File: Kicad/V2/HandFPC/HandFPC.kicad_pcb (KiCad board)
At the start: 2 copper layers, 25 parts, among them J10 SPI_LED, J2 JST_LED_SPI_5V_GND, J3 JST_LED_SPI_5V_GND, J4 JST_LED_SPI_5V_GND, J5 JST_LED_SPI_5V_GND, J6 JST_LED_SPI_5V_GND, J7 SPI_LED, J8 SPI_LED, J9 SPI_LED, U1 ICM-42688-P_I2C, U2 Hall Sensor DRV5023

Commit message: add edgecut for testing
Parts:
- moved J2 147.1 mm to (52.3, 183.0)
- moved FSR5 134.0 mm to (184.3, 97.4), turned to -90 degrees
- moved J3 130.2 mm to (58.8, 173.5)
- moved J4 124.7 mm to (70.6, 173.4)
- moved J5 123.6 mm to (82.0, 176.6)
- moved J6 123.1 mm to (95.3, 178.0)
- moved J10 122.8 mm to (166.1, 45.1), turned to -90 degrees
- moved C4 119.4 mm to (110.2, 152.1), turned to -90 degrees
- moved C1 113.3 mm to (93.5, 137.8), turned to -90 degrees
- moved C2 113.0 mm to (89.3, 141.5)
- moved U1 109.2 mm to (89.3, 137.6)
- moved J9 107.6 mm to (142.9, 10.5), turned to 180 degrees
- moved FSR1 106.9 mm to (17.5, 137.7)
- moved FSR4 103.0 mm to (165.8, 57.3), turned to 90 degrees
- moved C3 102.6 mm to (89.2, 133.4)
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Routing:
- net GND: track 0.00 -> 10.8 mm
- net +3.3V: track 0.00 -> 9.96 mm
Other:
- board outline added: 197.6 x 206 mm

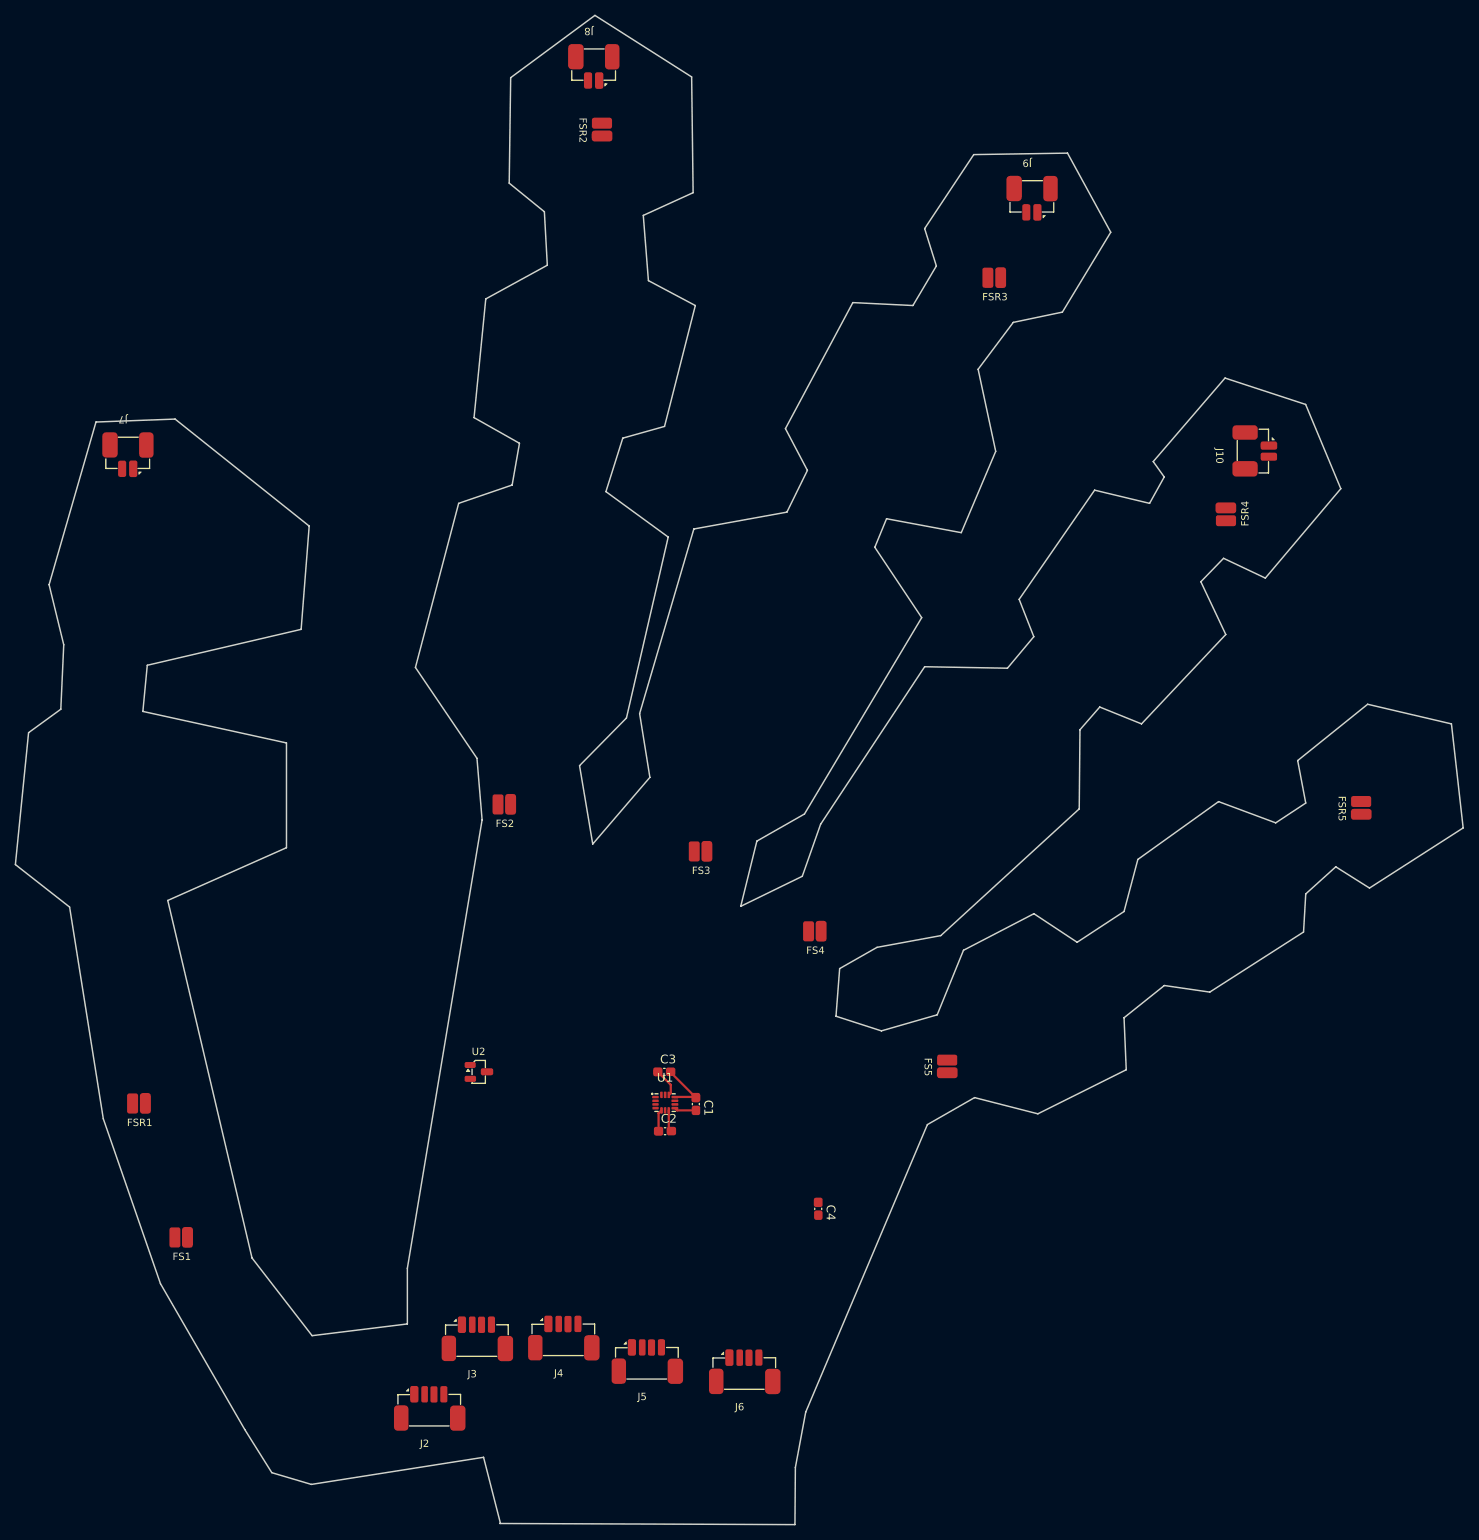
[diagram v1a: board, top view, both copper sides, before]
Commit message: start handfpc routing
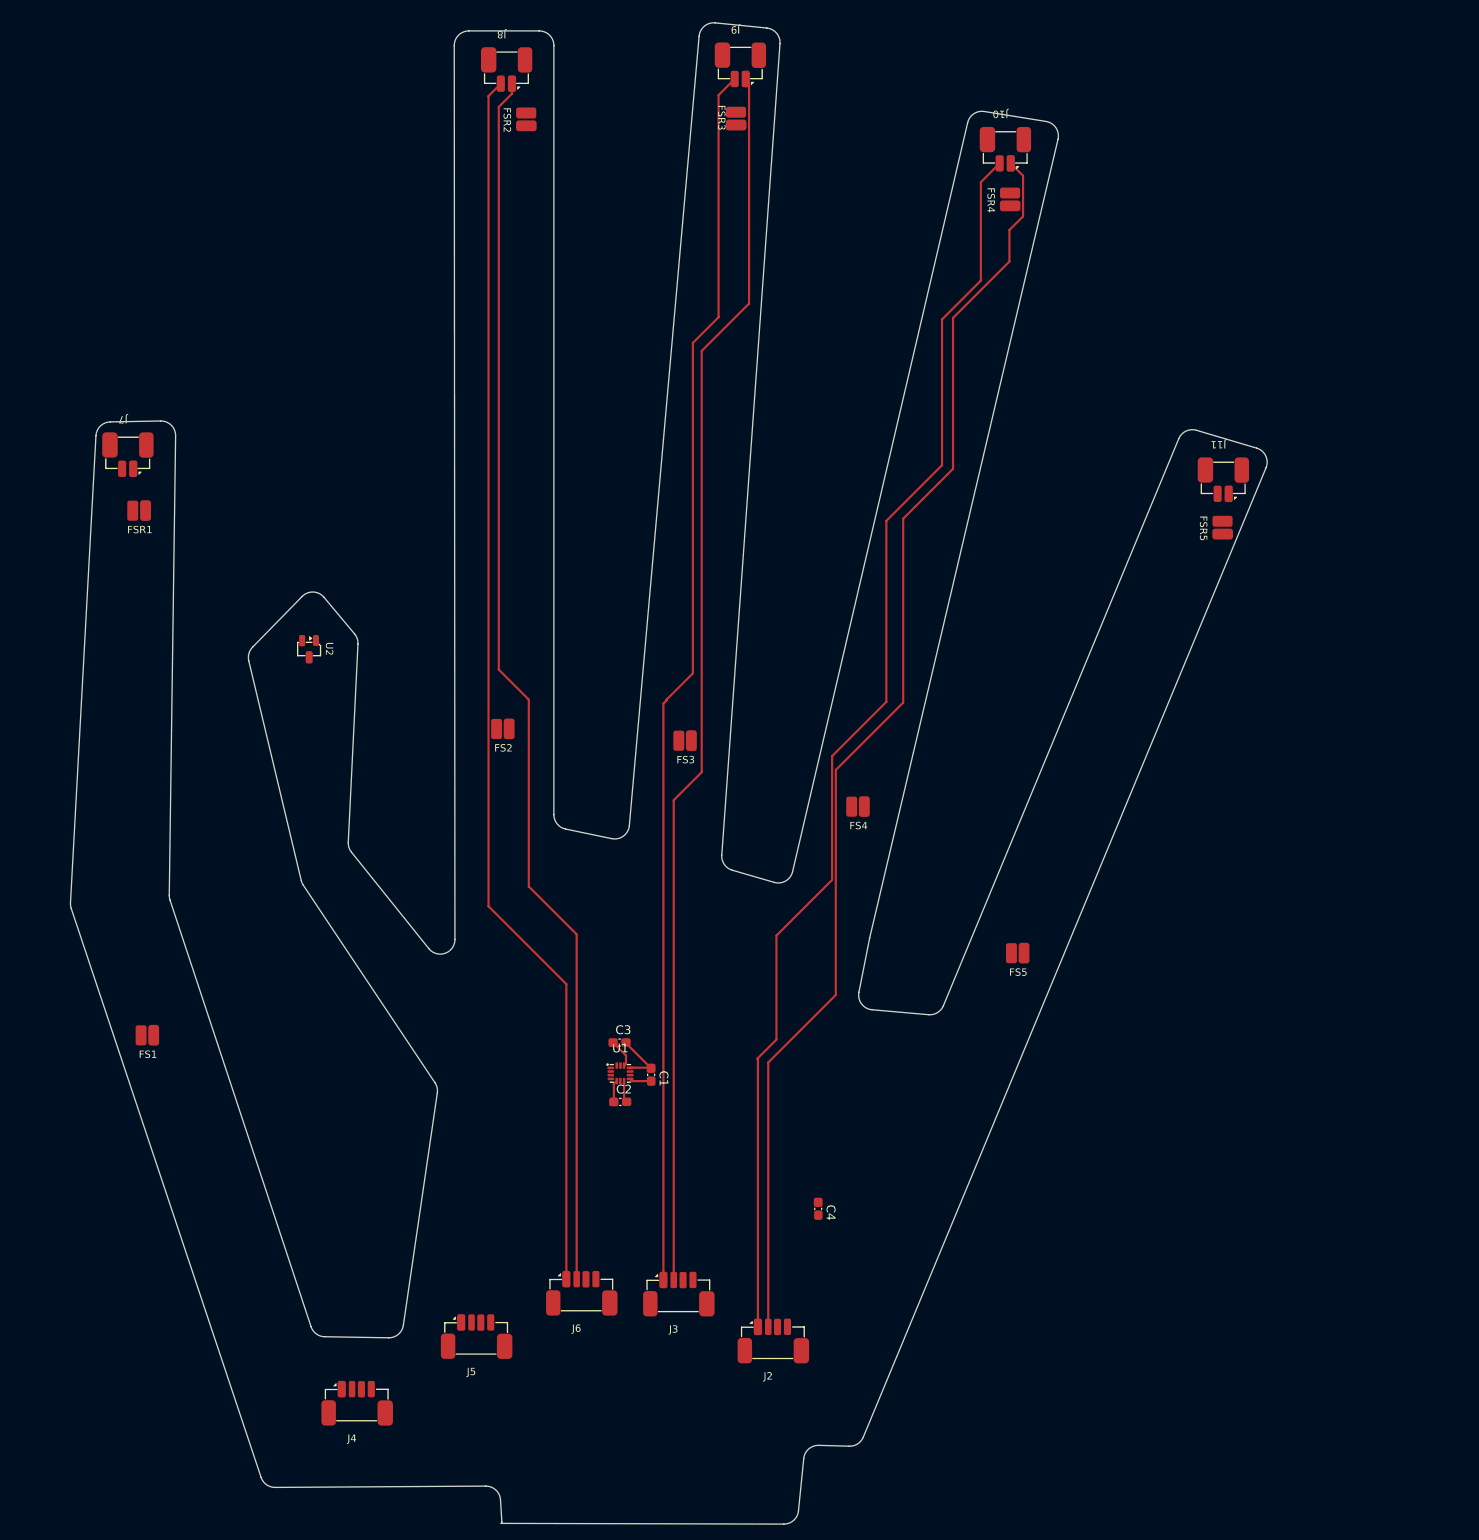
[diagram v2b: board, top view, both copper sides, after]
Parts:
- added J11: JST_SPI_LED_Out_Little, MyGlove:FPC_JST_Conn_GH_2x1.25mm, F.Cu at (169.0, 48.9)
- J10: value SPI_LED -> JST_SPI_LED_Out_Ring
- J2: value JST_LED_SPI_5V_GND -> JST_LED_SPI_In_Little
- J3: value JST_LED_SPI_5V_GND -> JST_LED_SPI_In_Ring
- J4: value JST_LED_SPI_5V_GND -> JST_LED_SPI_In_Thumb
- J5: value JST_LED_SPI_5V_GND -> JST_LED_SPI_In_Index
- J6: value JST_LED_SPI_5V_GND -> JST_LED_SPI_In_Major
- J7: value SPI_LED -> JST_SPI_LED_Out_Thumb
- J8: value SPI_LED -> JST_SPI_LED_Out_Index
- J9: value SPI_LED -> JST_SPI_LED_Out_Major
- moved FSR1 80.9 mm to (17.5, 56.8)
- moved U2 62.2 mm to (40.7, 75.7), turned to -90 degrees
- moved FSR4 52.1 mm to (136.4, 14.3), turned to -90 degrees
- moved J10 49.3 mm to (139.3, 3.84), turned to 180 degrees
- moved J2 47.8 mm to (99.2, 173.8)
- moved J9 43.8 mm to (103.1, -7.68)
- moved FSR5 42.7 mm to (165.4, 59.1)
- moved FSR3 41.4 mm to (99.0, 3.30), turned to -90 degrees
- moved J4 29.6 mm to (42.4, 182.3)
- moved J3 28.2 mm to (86.3, 167.4)
- moved FS1 28.0 mm to (18.7, 128.4)
- moved J6 24.7 mm to (73.0, 167.3)
- moved J5 23.5 mm to (58.7, 173.2)
- moved FS5 18.2 mm to (137.4, 117.2), turned to 0 degrees
- moved FS4 18.0 mm to (115.7, 97.2)
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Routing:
- net Net-(J10-Pad1): track 0.00 -> 173.9 mm
- net Net-(J10-Pad2): track 0.00 -> 172.5 mm
- net Net-(J3-Pad2): track 0.00 -> 168.4 mm
- net Net-(J6-Pad2): track 0.00 -> 168.3 mm
- net Net-(J6-Pad1): track 0.00 -> 168.3 mm
- net Net-(J3-Pad1): track 0.00 -> 167.9 mm
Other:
- board size 197.6 x 206 mm -> 163.3 x 204.9 mm

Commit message: add routing
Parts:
- added J1: FPC_Conn, MyGlove:FPC_Conn_24_GoldFinger, F.Cu at (126.0, 226.9)
- FS1, FS2, FS3, FS4, FS5: moved to B.Cu
- moved C4 81.4 mm to (56.8, 90.6), turned to 180 degrees
- moved J4 70.3 mm to (109.5, 203.0), turned to -90 degrees
- moved FSR1 66.8 mm to (39.8, 119.7), turned to 135 degrees
- moved J7 65.4 mm to (33.7, 109.3), turned to 0 degrees
- moved FS1 59.4 mm to (52.8, 177.0), turned to -120 degrees
- moved J2 57.4 mm to (150.4, 199.6), turned to 135 degrees
- moved J6 56.2 mm to (124.8, 189.0), turned to 180 degrees
- moved J3 55.5 mm to (137.3, 189.2), turned to 180 degrees
- moved FSR2 54.7 mm to (80.1, 57.2), turned to -45 degrees
- moved J8 53.4 mm to (71.1, 46.4), turned to 0 degrees
- moved J5 52.7 mm to (108.1, 191.6), turned to -135 degrees
- moved J9 44.7 mm to (103.3, 37.0), turned to 0 degrees
- moved FSR3 43.0 mm to (108.6, 45.2), turned to -45 degrees
- moved U1 41.5 mm to (117.3, 157.3), turned to 180 degrees
- moved C1 41.1 mm to (121.4, 156.8), turned to 180 degrees
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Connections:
- C4 pad 1: 5V -> +3.3V
- FS1 pad 2: 5V -> +3.3V
- FS2 pad 2: 5V -> +3.3V
- FS3 pad 2: 5V -> +3.3V
- FS4 pad 2: 5V -> +3.3V
- FS5 pad 2: 5V -> +3.3V
- FSR1 pad 2: 5V -> +3.3V
- FSR2 pad 2: 5V -> +3.3V
- FSR3 pad 2: 5V -> +3.3V
- FSR4 pad 2: 5V -> +3.3V
- FSR5 pad 2: 5V -> +3.3V
- U1 pad 1: unconnected-(U1-AP_AD0-Pad1) -> GND
- U2 pad 1: 5V -> +3.3V
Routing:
- net +3.3V: track 9.96 -> 677.5 mm, vias 0 -> 19
- net /FSR_Index/TouchADC: track 0.00 -> 233.2 mm
- net /FSR_Middle/TouchADC: track 0.00 -> 226.3 mm
- net /FSR_Ring/TouchADC: track 0.00 -> 197.9 mm
- net /Flex_Index/FlexADC: track 0.00 -> 184.0 mm, vias 0 -> 1
- net /FSR_Little/TouchADC: track 0.00 -> 176.6 mm
- net /Flex_Middle/FlexADC: track 0.00 -> 165.3 mm, vias 0 -> 1
- net Net-(J5-Pad2): track 0.00 -> 143.6 mm
- net Net-(J5-Pad1): track 0.00 -> 142.5 mm
- net /Flex_Ring/FlexADC: track 0.00 -> 141.8 mm, vias 0 -> 1
- net /Flex_Little/FlexADC: track 0.00 -> 124.9 mm, vias 0 -> 1
- net GND: track 10.8 -> 135.2 mm, vias 0 -> 17
- net 5VL: track 0.00 -> 82.1 mm
- net /IMU_1/IMU_I2C_SDA: track 0.00 -> 70.3 mm, vias 0 -> 2
- net /IMU_1/IMU_I2C_SCL: track 0.00 -> 70.2 mm, vias 0 -> 2
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- added copper zone on B.Cu, net GND
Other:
- board size 163.3 x 204.9 mm -> 144.5 x 199.6 mm

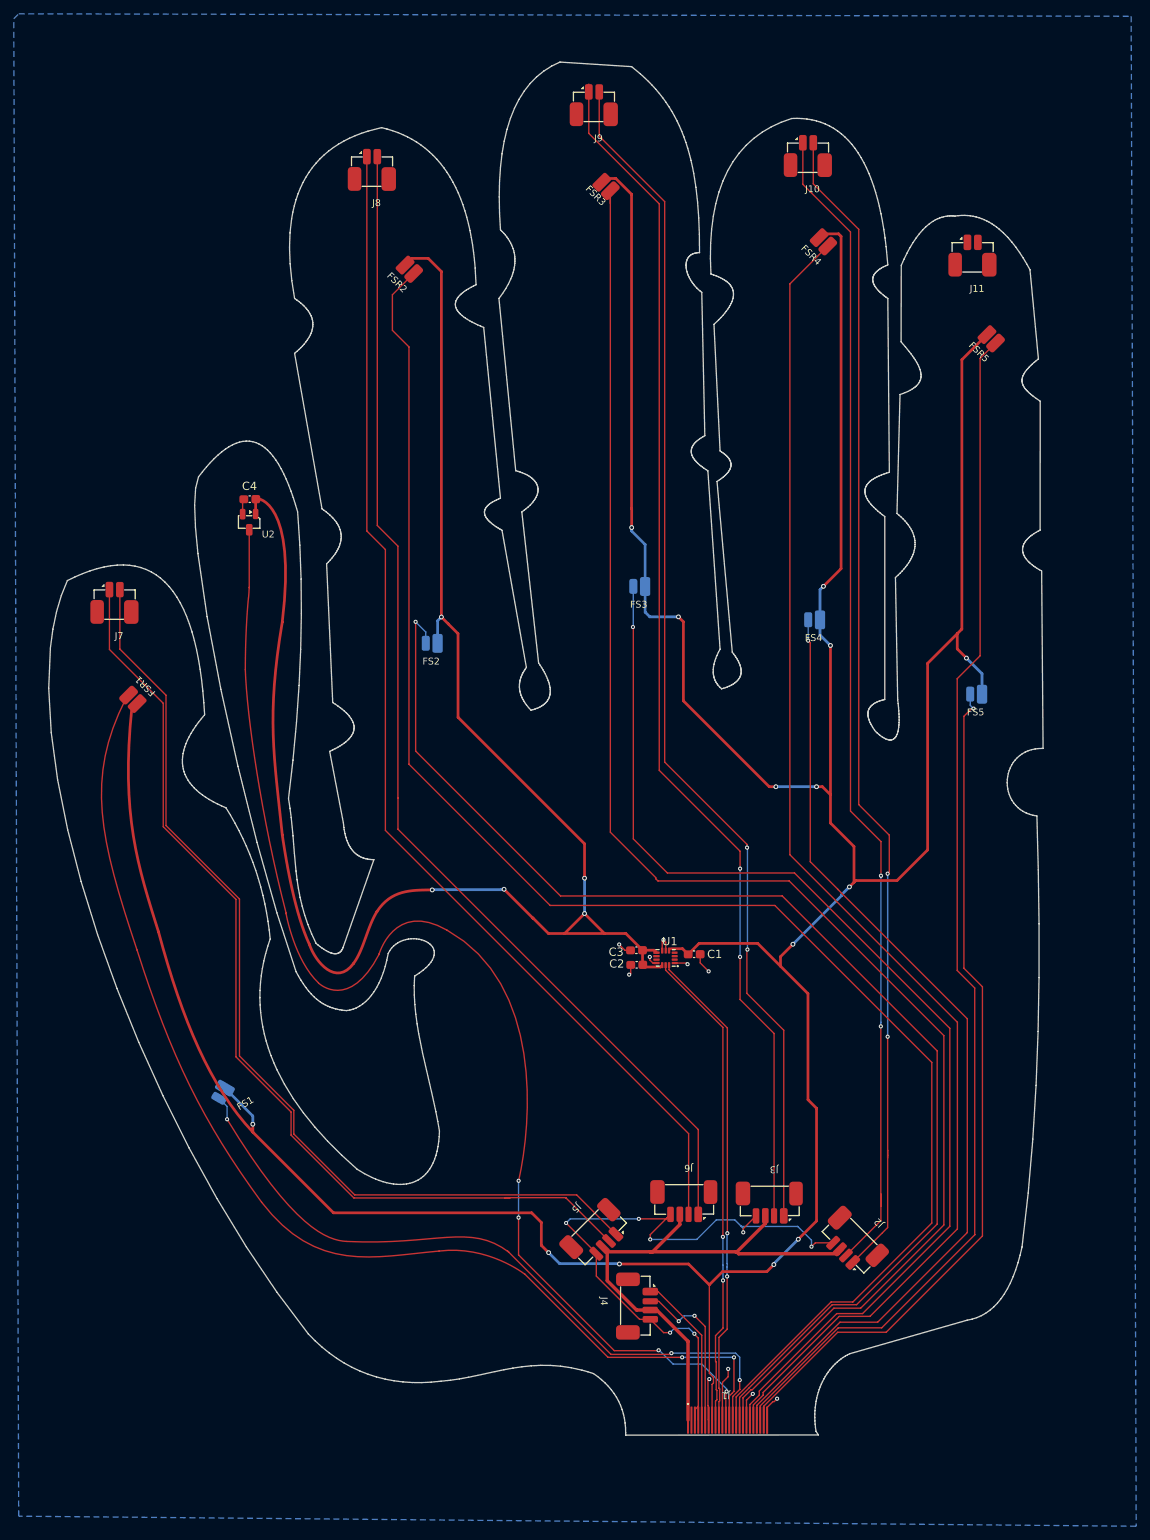
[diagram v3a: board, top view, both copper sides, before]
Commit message: add upper gnd pour
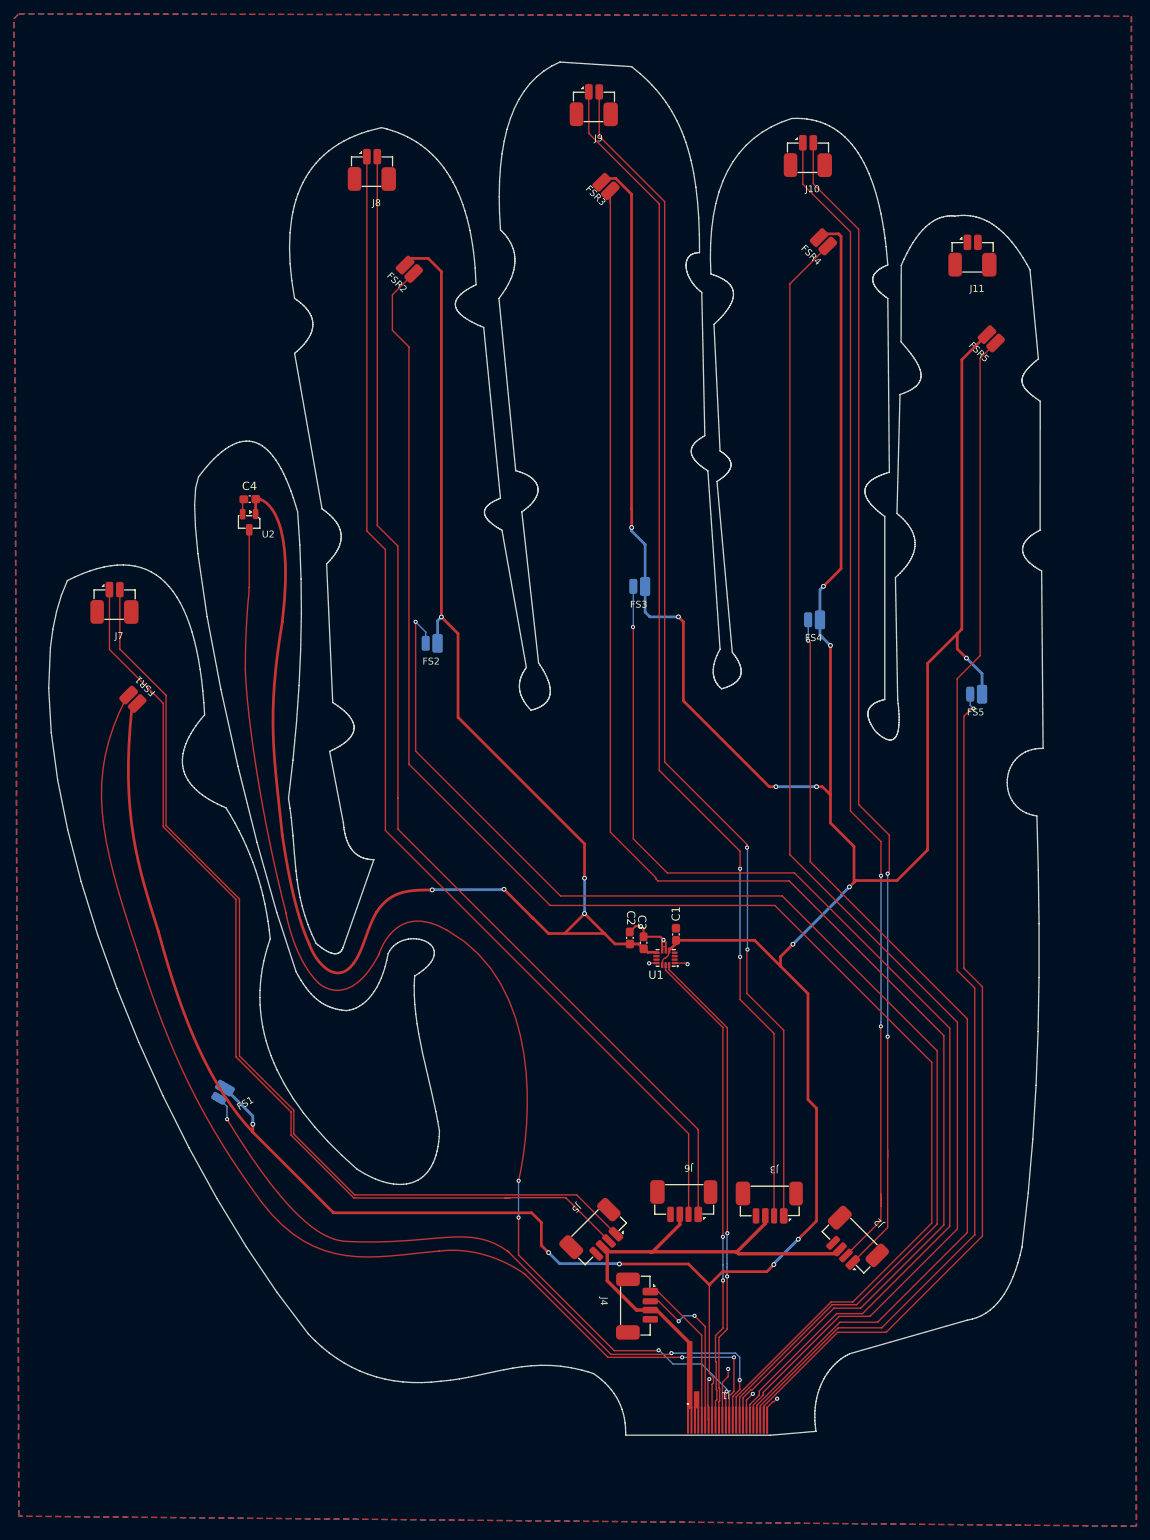
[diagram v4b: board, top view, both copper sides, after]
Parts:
- moved C2 4.04 mm to (112.1, 154.4), turned to 90 degrees
- moved C1 3.90 mm to (118.8, 153.9), turned to -90 degrees
- moved C3 1.52 mm to (114.1, 155.1), turned to 90 degrees
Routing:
- net GND: track 135.2 -> 38.8 mm, vias 17 -> 8
- net 5VL: track 82.1 -> 70.6 mm
- net +3.3V: track 677.5 -> 672.6 mm
- added copper zone on F.Cu, net GND
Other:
- outline, holes or cut-outs redrawn
